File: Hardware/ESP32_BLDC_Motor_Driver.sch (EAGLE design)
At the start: 110 parts, among them J1 USB-C Connector, J2 0532610371, J3 POWER_JACKPOWER_JACK_SLOT, J4 Breadboard Connector, J5 Breadboard Headers, J6 0.1in header, J7 QWIIC_RIGHT_ANGLE, J8 Breakout Header, Q1 20V/4.2A/52mΩ/1.4W, Q2 NPN Transistors, U1 TMC6300, U3 ESP-WROOM-3232D-NARROW, U4 CH340C, U5 ESD Diode, U6 AP63357, U7 AP2202-ADJ, U8 TMAG5273, U9 LMV324

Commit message: Updates to schematic and layout as per design review checklist
Finished design errors- close to design review
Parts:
- added R29, R30, R31: 0.015ohm, SparkFun-Resistors:0.015OHM_1%_1/3W_0603
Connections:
- removed net ESP_12/GPIO1: J4.7, U3.POCI2/IOA12
- removed net ESP_15/GPIO4: J4.6, U3.CS2/IOA15
- removed net ESP_5/GPIO5: J4.8, U3.CS3/IO5
- removed net N$6: U9G2.-IN
- new net ESP_12/V_OUT: J4.7, U3.POCI2/IOA12, U9G3.OUT
- new net ESP_15/W_OUT: J4.6, U3.CS2/IOA15, U9G4.OUT
- new net ESP_5/U_OUT: J4.8, U3.CS3/IO5, U9G2.OUT
- new net SENSE_U: R29.1, U1.U, U9G2.-IN
- new net SENSE_V: R30.1, U1.V, U9G3.-IN
- new net SENSE_W: R31.1, U1.W, U9G4.-IN
- net U: now also R29.2, U9G2.+IN; no longer U1.U
- net V: now also R30.2, U9G3.+IN; no longer U1.V
- net W: now also R31.2, U9G4.+IN; no longer U1.W
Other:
- moved on the sheet: C3, J2, J6, R20, R21, U9G1, U9G2, U9G3, U9G4, U9G5

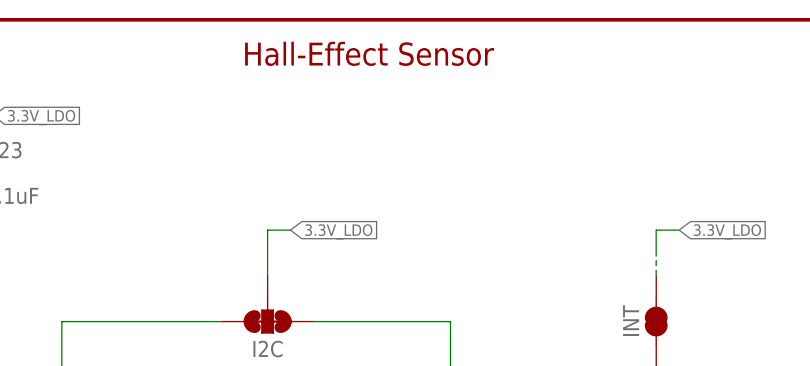
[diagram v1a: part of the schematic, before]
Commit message: Updates for Design Review
Added more silk for buttons and outputs; added datasheet for correct Op Amp and deleted the old one; adjusted MOLEX output connector to motor for better connectivity and less strain on the cable; changed version number to v01; added more GND vias
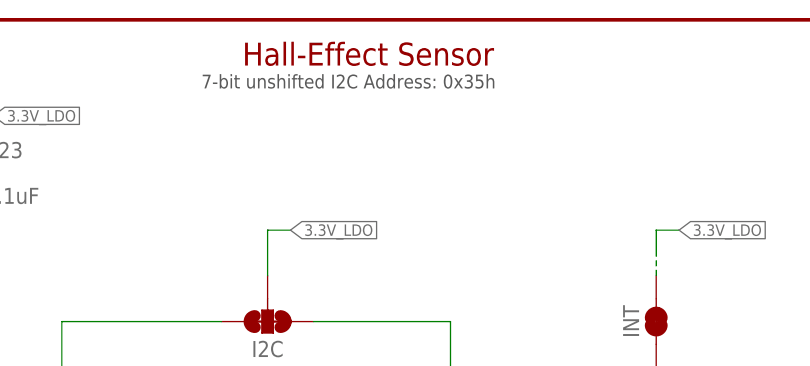
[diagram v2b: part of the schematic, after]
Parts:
- LOGO4: value QWIIC_LOGO_3MM -> QWIIC_LOGO_5MM; device SparkFun-Aesthetics:QWIIC_LOGO_3MM -> SparkFun-Aesthetics:QWIIC_LOGO_5MM
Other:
- note added: "7-bit unshifted I2C Address: 0x35h"
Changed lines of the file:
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@@
 <grid distance="0.1" unitdist="inch" unit="inch" style="lines" multiple="1" display="no" altdistance="0.01" altunitdist="inch" altunit="inch"/>
 <layers>
-<layer number="1" name="Top" color="4" fill="1" visible="no" active="no"/>
-<layer number="2" name="Route2" color="58" fill="1" visible="no" active="no"/>
-<layer number="15" name="Route15" color="29" fill="1" visible="no" active="no"/>
-<layer number="16" name="Bottom" color="1" fill="1" visible="no" active="no"/>
-<layer number="17" name="Pads" color="2" fill="1" visible="no" active="no"/>
-<layer number="18" name="Vias" color="2" fill="1" visible="no" active="no"/>
-<layer number="19" name="Unrouted" color="6" fill="1" visible="no" active="no"/>
-<layer number="20" name="Dimension" color="24" fill="1" visible="no" active="no"/>
-<layer number="21" name="tPlace" color="16" fill="1" visible="no" active="no"/>
-<layer number="22" name="bPlace" color="14" fill="1" visible="no" active="no"/>
-<layer number="23" name="tOrigins" color="15" fill="1" visible="no" active="no"/>
-<layer number="24" name="bOrigins" color="15" fill="1" visible="no" active="no"/>
-<layer number="25" name="tNames" color="7" fill="1" visible="no" active="no"/>
-<layer number="26" name="bNames" color="7" fill="1" visible="no" active="no"/>
-<layer number="27" name="tValues" color="7" fill="1" visible="no" active="no"/>
-<layer number="28" name="bValues" color="7" fill="1" visible="no" active="no"/>
+<layer number="1" name="Top" color="4" fill="1" visible="yes" active="no"/>
+<layer number="2" name="Route2" color="58" fill="1" visible="yes" active="no"/>
+<layer number="15" name="Route15" color="29" fill="1" visible="yes" active="no"/>
+<layer number="16" name="Bottom" color="1" fill="1" visible="yes" active="no"/>
+<layer number="17" name="Pads" color="2" fill="1" visible="yes" active="no"/>
+<layer number="18" name="Vias" color="2" fill="1" visible="yes" active="no"/>
+<layer number="19" name="Unrouted" color="6" fill="1" visible="yes" active="no"/>
+<layer number="20" name="Dimension" color="24" fill="1" visible="yes" active="no"/>
+<layer number="21" name="tPlace" color="16" fill="1" visible="yes" active="no"/>
+<layer number="22" name="bPlace" color="14" fill="1" visible="yes" active="no"/>
+<layer number="23" name="tOrigins" color="15" fill="1" visible="yes" active="no"/>
+<layer number="24" name="bOrigins" color="15" fill="1" visible="yes" active="no"/>
+<layer number="25" name="tNames" color="7" fill="1" visible="yes" active="no"/>
+<layer number="26" name="bNames" color="7" fill="1" visible="yes" active="no"/>
+<layer number="27" name="tValues" color="7" fill="1" visible="yes" active="no"/>
+<layer number="28" name="bValues" color="7" fill="1" visible="yes" active="no"/>
 <layer number="29" name="tStop" color="7" fill="3" visible="no" active="no"/>
 <layer number="30" name="bStop" color="7" fill="6" visible="no" active="no"/>
@@
 <layer number="35" name="tGlue" color="7" fill="4" visible="no" active="no"/>
 <layer number="36" name="bGlue" color="7" fill="5" visible="no" active="no"/>
-<layer number="37" name="tTest" color="7" fill="1" visible="no" active="no"/>
-<layer number="38" name="bTest" color="7" fill="1" visible="no" active="no"/>
+<layer number="37" name="tTest" color="7" fill="1" visible="yes" active="no"/>
+<layer number="38" name="bTest" color="7" fill="1" visible="yes" active="no"/>
 <layer number="39" name="tKeepout" color="4" fill="11" visible="no" active="no"/>
 <layer number="40" name="bKeepout" color="1" fill="11" visible="no" active="no"/>
@@
 <layer number="44" name="Drills" color="7" fill="1" visible="no" active="no"/>
 <layer number="45" name="Holes" color="7" fill="1" visible="no" active="no"/>
-<layer number="46" name="Milling" color="3" fill="1" visible="no" active="no"/>
-<layer number="47" name="Measures" color="7" fill="1" visible="no" active="no"/>
-<layer number="48" name="Document" color="7" fill="1" visible="no" active="no"/>
-<layer number="49" name="Reference" color="7" fill="1" visible="no" active="no"/>
-<layer number="50" name="dxf" color="7" fill="1" visible="no" active="no"/>
-<layer number="51" name="tDocu" color="6" fill="1" visible="no" active="no"/>
-<layer number="52" name="bDocu" color="7" fill="1" visible="no" active="no"/>
-<layer number="53" name="tGND_GNDA" color="7" fill="9" visible="no" active="no"/>
-<layer number="54" name="bGND_GNDA" color="1" fill="9" visible="no" active="no"/>
-<layer number="56" name="wert" color="7" fill="1" visible="no" active="no"/>
-<layer number="57" name="tCAD" color="7" fill="1" visible="no" active="no"/>
-<layer number="58" name="bCAD" color="7" fill="1" visible="no" active="no"/>
-<layer number="59" name="tCarbon" color="7" fill="1" visible="no" active="no"/>
-<layer number="60" name="bCarbon" color="7" fill="1" visible="no" active="no"/>
+<layer number="46" name="Milling" color="3" fill="1" visible="yes" active="no"/>
+<layer number="47" name="Measures" color="7" fill="1" visible="yes" active="no"/>
+<layer number="48" name="Document" color="7" fill="1" visible="yes" active="no"/>
+<layer number="49" name="Reference" color="7" fill="1" visible="yes" active="no"/>
+<layer number="50" name="dxf" color="7" fill="1" visible="yes" active="no"/>
+<layer number="51" name="tDocu" color="6" fill="1" visible="yes" active="no"/>
+<layer number="52" name="bDocu" color="7" fill="1" visible="yes" active="no"/>
+<layer number="53" name="tGND_GNDA" color="7" fill="9" visible="yes" active="no"/>
+<layer number="54" name="bGND_GNDA" color="1" fill="9" visible="yes" active="no"/>
+<layer number="56" name="wert" color="7" fill="1" visible="yes" active="no"/>
+<layer number="57" name="tCAD" color="7" fill="1" visible="yes" active="no"/>
+<layer number="58" name="bCAD" color="7" fill="1" visible="yes" active="no"/>
+<layer number="59" name="tCarbon" color="7" fill="1" visible="yes" active="no"/>
+<layer number="60" name="bCarbon" color="7" fill="1" visible="yes" active="no"/>
 <layer number="88" name="SimResults" color="9" fill="1" visible="yes" active="yes"/>
 <layer number="89" name="SimProbes" color="9" fill="1" visible="yes" active="yes"/>
@@
 <part name="SUPPLY12" library="SparkFun-PowerSymbols" deviceset="VIN" device=""/>
 <part name="GND43" library="SparkFun-PowerSymbols" deviceset="GND" device=""/>
-<part name="LOGO4" library="SparkFun-Aesthetics" deviceset="QWIIC_LOGO" device="_3MM"/>
+<part name="LOGO4" library="SparkFun-Aesthetics" deviceset="QWIIC_LOGO" device="_5MM" value="QWIIC_LOGO_5MM"/>
 <part name="TP2" library="SparkFun-Connectors" deviceset="TEST-POINT" device="3X4"/>
 <part name="TP3" library="SparkFun-Connectors" deviceset="TEST-POINT" device="3X4"/>
@@
 <wire x1="264.16" y1="200.66" x2="431.8" y2="200.66" width="0.2032" layer="97" style="longdash"/>
 <text x="39.878" y="116.84" size="1.524" layer="97" font="vector">Maximum Input Current: 0.5A</text>
+<text x="352.298" y="271.78" size="1.524" layer="97" font="vector">7-bit unshifted I2C Address: 0x35h</text>
 </plain>
 <instances>

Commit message: Design Updates from design review - schematic changes mostly
***Changes are still not done*** Changes can be seen detailed in the protos design review; changed TMAG5273 symbol to be correct
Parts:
- removed R29, R30, R31: 0.015ohm, SparkFun-Resistors:0.015OHM_1%_1/3W_0603
- added MOTOR: JUMPER-SMT_2_NC_TRACE_SILK, SparkFun-Jumpers:JUMPER-SMT_2_NC_TRACE_SILK
- added R32, R33, R34: 0.012ohm, SparkFun-Resistors:0.012OHM0603
- added TP10, TP11, TP12: TEST-POINT3X4, SparkFun-Connectors:TEST-POINT3X4
- J4, J5: device SparkFun-Connectors:CONN_08" -> SparkFun-Connectors:CONN_08NO_SILK_DNP
- R17: value 100k -> 4.7k; device SparkFun-Resistors:100KOHM-0603-1/10W-1% -> SparkFun-Resistors:4.7KOHM-0603-1/10W-1%
- U3: value ESP-WROOM-3232D-NARROW -> ESP-WROOM-3232D; device SparkFun-RF:ESP-WROOM-3232D-NARROW -> SparkFun-RF:ESP-WROOM-3232D
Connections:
- net ESP_4/!INT renamed ESP_4/!INT_MAG
- removed net 3.3V_LDO: C1.1, C17.1, C22.1, C23.1, C3.1, C4.1, C9.1, I2C.2, INT.2, J7.2, R16.2, R22.2, STAT.VCC, U3.3V3, U4.V3, U4.VCC, U7.OUT, U8.VCC, U9G5.P$V+
- removed net ESP_17/EN: R24.1, U3.IO17, U7.EN
- new net 3.3V_A: C1.1, C17.1, C22.1, C23.1, C3.1, C4.1, C9.1, I2C.2, INT.2, J7.2, PWR.2, R16.2, R22.2, STAT.VCC, U3.3V3, U4.V3, U4.VCC, U7.OUT, U8.VCC, U9G5.P$V+
- new net ESP_12/LED: STAT.DI, U3.POCI2/IOA12
- new net ESP_17/________: U3.IO17
- new net ESP_36/V_OUT: U3.SENSOR_VP/IA36, U9G3.OUT
- new net ESP_39/W_OUT: U3.SENSOR_VN/IA39, U9G4.OUT
- new net LDO_EN: R24.1, U7.EN
- new net N$10: R27.1, U8.SDA
- new net N$16: PWR.1, R17.2
- new net N$6: R26.1, U8.SCL
- net 3.3V: now also MOTOR.2; no longer PWR.2
- net ESP_12/V_OUT: now also TP11.1; no longer U3.POCI2/IOA12, U9G3.OUT
- net ESP_15/W_OUT: now also TP12.1; no longer U9G4.OUT
- net ESP_16/EN_MOTOR_PWR: no longer R17.1
- net ESP_21/TP_SDA: no longer R26.1, U8.SDA
- net ESP_22/TP_SCL: no longer R27.1, U8.SCL
- net ESP_36/LED: no longer STAT.DI, U3.SENSOR_VP/IA36
- net ESP_39/TP_A3: no longer U3.SENSOR_VN/IA39
- net ESP_5/U_OUT: now also TP10.1
- net GND: now also R17.1, U8.TEST; no longer U8.GND(TEST)
- net N$12: now also R26.2; no longer R27.2
- net N$13: now also R27.2; no longer R26.2
- net N$23: now also MOTOR.1; no longer PWR.1
- net SENSE_U: now also R32.1; no longer R29.1
- net SENSE_V: now also R33.1; no longer R30.1
- net SENSE_W: now also R34.1; no longer R31.1
- net U: now also R32.2; no longer R29.2
- net V: now also R33.2; no longer R30.2
- net VIN: no longer R17.2
- net W: now also R34.2; no longer R31.2
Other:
- note added: "20V/4.2A/1.4W"
- note added: "3.3V_A is the alternate voltage supply on board"
- note added: "Cut Jumper MOTOR to disable Motor Power LED"
- note added: "D7 is used to protect the circuit from over- voltage"
- note added: "Motor Power Supply"
- note added: "Vin Range: 4V - 15V"
- note removed: "Power Supply"
- note removed: "Vin Range: 6V - 15V"
- moved on the sheet: BYP, C1, C10, C11, C12, C13, C14, C15, C16, C17, C18, C19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

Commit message: Updates for design review
Fixed schematic - reordering ESP_32 pinouts, breakout headers, adjusted inline current sensing; re-completed layout - repositioned placement of power scheme and input connectors, swapped placement of motor and motor driver/current sensors; fixed screw hole size of the motor; fixed schematic symbol for hall effect sensor.
For a full list, see design review document
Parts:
- removed C12, C13, C14, C15: 0.1uF, SparkFun-Capacitors:0.1UF-0603-25V-(+80/-20%)
- removed D8: RED, SparkFun-LED:LED-RED_0603-KB
- removed R25: 10k, SparkFun-Resistors:10KOHM-0603-1/10W-1%
- added D2, MPWR: RED, SparkFun-LED:LED-RED_0603-KB
- added R29, R30, R40, R41, R42, R43: 20k, SparkFun-Resistors:20KOHM-0603-1/10W-1%
- added R31, R35, R36, R37, R38, R39: 1k, SparkFun-Resistors:1KOHM-0603-1/10W-1%
- S1, S2, S3, S4: value MOMENTARY-SWITCH-SPST-SMD-4.6X2.8MM -> (none); device SparkFun-Switches:MOMENTARY-SWITCH-SPST-SMD-4.6X2.8MM -> SparkFun-Switches:MOMENTARY-SWITCH-SPST-2-SMD-5.2MM-TALL
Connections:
- removed net ESP_0/!STDBY: J5.2, S.2, U1.VIO/!STDBY!, U3.IOA2
- removed net ESP_12/LED: STAT.DI, U3.POCI2/IOA12
- removed net ESP_12/V_OUT: J4.7, TP11.1
- removed net ESP_13/UH: R12.2, TP3.1, U1.UH, U3.PICO2/IOA13
- removed net ESP_14/UL: R11.2, TP4.1, U1.UL, U3.SCK2/IOA14
- removed net ESP_15/W_OUT: J4.6, TP12.1, U3.CS2/IOA15
- removed net ESP_16/EN_MOTOR_PWR: U3.IO16, U6.EN
- removed net ESP_17/________: U3.IO17
- removed net ESP_18/DIAG: D.2, U1.DIAG, U3.SCK3/IO18
- removed net ESP_19/POCI: J4.4, U3.POCI3/IO19
- removed net ESP_23/PICO: J4.3, U3.PICO3/IO23
- removed net ESP_25/WH: R8.2, TP7.1, U1.WH, U3.DAC1/IOA25
- removed net ESP_26/VL: R9.2, TP6.1, U1.VL, U3.DAC2/IOA26
- removed net ESP_27/VH: R10.2, TP5.1, U1.VH, U3.IOA27
- removed net ESP_36/LED: J5.6
- removed net ESP_39/TP_A3: J5.5
- removed net ESP_5/U_OUT: J4.8, TP10.1, U3.CS3/IO5, U9G2.OUT
- removed net N$10: R27.1, U8.SDA
- removed net N$6: R26.1, U8.SCL
- new net ESP_12/GPIO1: J4.8, U3.POCI2/IOA12
- new net ESP_13/U_OUT: R35.2, TP10.1, U3.PICO2/IOA13, U9G2.OUT
- new net ESP_14/DIAG: D.2, U1.DIAG, U3.SCK2/IOA14
- new net ESP_15/GPIO4: J4.7, U3.CS2/IOA15
- new net ESP_16/UH: R12.2, TP3.1, U1.UH, U3.IO16
- new net ESP_17/UL: R11.2, TP4.1, U1.UL, U3.IO17
- new net ESP_18/VH: R10.2, TP5.1, U1.VH, U3.SCK3/IO18
- new net ESP_19/WH: R8.2, TP7.1, U1.WH, U3.POCI3/IO19
- new net ESP_2/RGB_DI: J5.6, STAT.DI, TP1.1, U3.IOA2
- new net ESP_23/VL: R9.2, TP6.1, U1.VL, U3.PICO3/IO23
- new net ESP_25/TP_A1: J4.5, U3.DAC1/IOA25
- new net ESP_26/TP_A0: J4.4, U3.DAC2/IOA26
- new net ESP_27/GPIO2: J4.3, U3.IOA27
- new net ESP_5/!STDBY: S.2, U1.VIO/!STDBY!, U3.CS3/IO5
- new net MOTOR_EN: J4.6, U6.EN
- new net N$16: R29.2, R35.1, U9G2.-IN
- new net N$18: R30.2, R31.1, U9G2.+IN
- new net N$19: R36.1, R40.2, U9G3.-IN
- new net N$20: R38.1, R43.2, U9G3.+IN
- new net N$24: R37.1, R41.2, U9G4.-IN
- new net N$25: R39.1, R42.2, U9G4.+IN
- new net N$9: D2.A, R17.1
- net !RESET: now also S2.1; no longer C13.1
- net 3.3V: now also C23.1, C3.1, I2C.2, INT.2, U8.VCC, U9G5.P$V+
- net 3.3V_A: no longer C23.1, C3.1, I2C.2, INT.2, U8.VCC, U9G5.P$V+
- net ESP_0/QPWR: now also J5.2, S1.1; no longer C12.1, TP1.1
- net ESP_21/TP_SDA: now also R27.1, U8.SDA
- net ESP_22/TP_SCL: now also R26.1, U8.SCL
- net ESP_34/AUX1: now also J5.7, S3.1, S3.2; no longer C14.1, J5.8, S4.2
- net ESP_35/AUX2: now also J5.8, S4.1, S4.2; no longer C15.1, J5.7, S3.2
- net ESP_36/V_OUT: now also R36.2, TP11.1
- net ESP_39/W_OUT: now also R37.2, TP12.1
- net ESP_4/!INT_MAG: now also J5.5; no longer J4.5
- net GND: now also D2.C, J3.GND, MPWR.C, R31.2, R38.2, R39.2, S1.3, S1.4, S2.3, S2.4, S3.3, S3.4, S4.3, S4.4; no longer C12.2, C13.2, C14.2, C15.2, D8.C, J3.GNDBREAK, R17.1, R25.1, S1.1, S2.1, S3.1, S4.1
- net N$34: now also MPWR.A; no longer D8.A
- net N$5: now also J3.GNDBREAK; no longer J3.GND
- net SENSE_U: now also R30.1; no longer U9G2.-IN
- net SENSE_V: now also R43.1; no longer U9G3.-IN
- net SENSE_W: now also R42.1; no longer U9G4.-IN
- net U: now also R29.1; no longer U9G2.+IN
- net V: now also R40.1; no longer U9G3.+IN
- net V_USB: no longer R25.2
- net W: now also R41.1; no longer U9G4.+IN
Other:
- note added: "MPWR"
- note added: "Motor Current Sensing"
- moved on the sheet: C10, C11, C16, C18, C19, C2, C20, C21, C23, C3, C4, C5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
